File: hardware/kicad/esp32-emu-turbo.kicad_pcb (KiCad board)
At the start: 4 copper layers, 160 x 75 mm, 88 parts, among them J1 USB-C-16P, J3 JST-PH-2P-SMD, J4 FPC-40P-0.5mm, SW1 SW-SMD-5.1x5.1, SW10 SW-SMD-5.1x5.1, SW11 SW-SMD-5.1x5.1, SW12 SW-SMD-5.1x5.1, SW13 SW-SMD-5.1x5.1, SW2 SW-SMD-5.1x5.1, SW3 SW-SMD-5.1x5.1, SW4 SW-SMD-5.1x5.1, SW5 SW-SMD-5.1x5.1, SW6 SW-SMD-5.1x5.1, SW7 SW-SMD-5.1x5.1, SW8 SW-SMD-5.1x5.1, SW9 SW-SMD-5.1x5.1, U1 ESP32-S3-WROOM-1-N16R8, U2 ESOP-8, U3 SOT-223, U4 SOT-23-6, U5 SOP-16, U6 TF-01A

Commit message: feat(pcb+fw): add BAT54C menu combo diode — SW13 triggers START+SELECT
Hardware: D1 BAT54C dual Schottky (SOT-23, C8655) connects SW13 menu
button to BTN_START and BTN_SELECT via diode isolation. Pressing SW13
pulls both signals LOW simultaneously; firmware detects combo as MENU.
Includes SOT-23-3 footprint, MENU_K cathode net, routing, BOM/CPL/gerbers.

Firmware: BTN_MENU_COMBO macro + input_menu_pressed() combo detector.

Fixes: BTN_R jog clearance for SW13 GND pads, U5 VREF datasheet spec,
BTN_MENU orphan net in design-intent checker.

DFM: 115/115 pass, DFA: 9/9 pass, design intent: 363/363 pass.

Co-Authored-By: Claude Opus 4.6 (1M context) <noreply@anthropic.com>
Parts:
- removed the C26 at (91.5, 21.0)
- removed the C3 at (69.5, 42.0)
- removed the C4 at (92.0, 42.0)
- removed the J3 at (80.0, 62.5)
- removed the R17 at (25.0, 65.0)
- removed the R18 at (32.0, 65.0)
- removed the R22 at (90.2, 40.0)
- removed the R23 at (91.7, 38.5)
- removed the R3 at (65.0, 42.0)
- removed the SW7 at (142.0, 42.5)
- added C1: C_0805, C_0805, B.Cu at (120.0, 57.0)
- added C2: C_1206, C_1206, B.Cu at (125.0, 62.5)
- added C21: C_0805, C_0805, B.Cu at (38.0, 23.5)
- added C22: C_0805, C_0805, B.Cu at (33.2, 20.0)
- added C23: C_0805, C_0805, B.Cu at (38.0, 29.5)
- added C24: C_0805, C_0805, B.Cu at (29.4, 22.0)
- added C25: C_0805, C_0805, B.Cu at (31.5, 37.5)
- added D1: SOT-23-3, SOT-23-3, B.Cu at (156.0, 52.5)
- added FID3: Fiducial, Fiducial, F.Cu at (12.0, 63.0)
- added LED1: LED_0805, LED_0805, F.Cu at (25.0, 67.5)
- added R21: R_0805, R_0805, B.Cu at (38.0, 32.5)
- C11: renamed from C19; value C_1206 -> C_0805; footprint C_1206 -> C_0805
- C14: renamed from R20; value R_0805 -> C_0805; footprint R_0805 -> C_0805
- C15: renamed from R21; value R_0805 -> C_0805; footprint R_0805 -> C_0805
- C19: renamed from C1; value C_0805 -> C_1206; footprint C_0805 -> C_1206
- C26: renamed from R10; value R_0805 -> C_0805; footprint R_0805 -> C_0805
- C27: renamed from C2; value C_1206 -> C_0805; footprint C_1206 -> C_0805
- C3: renamed from R8; value R_0805 -> C_0805; footprint R_0805 -> C_0805
- C4: renamed from R9; value R_0805 -> C_0805; footprint R_0805 -> C_0805
- J3: renamed from U4; value SOT-23-6 -> JST-PH-2P-SMD; footprint SOT-23-6 -> JST-PH-2P-SMD
- R10: renamed from C6; value C_0805 -> R_0805; footprint C_0805 -> R_0805
- R11: renamed from C7; value C_0805 -> R_0805; footprint C_0805 -> R_0805
- R12: renamed from C8; value C_0805 -> R_0805; footprint C_0805 -> R_0805
- R13: renamed from C9; value C_0805 -> R_0805; footprint C_0805 -> R_0805
- R14: renamed from C10; value C_0805 -> R_0805; footprint C_0805 -> R_0805
- R15: renamed from C11; value C_0805 -> R_0805; footprint C_0805 -> R_0805
- R16: renamed from C13; value C_0805 -> R_0805; footprint C_0805 -> R_0805
- R19: renamed from C12; value C_0805 -> R_0805; footprint C_0805 -> R_0805
- R20: renamed from FID3; value Fiducial -> R_0805; footprint Fiducial -> R_0805; moved to B.Cu
- R22: renamed from R5; value R_0805 -> R_0402; footprint R_0805 -> R_0402
- R23: renamed from R6; value R_0805 -> R_0402; footprint R_0805 -> R_0402
- R9: renamed from C5; value C_0805 -> R_0805; footprint C_0805 -> R_0805
- SW7: renamed from LED1; value LED_0805 -> SW-SMD-5.1x5.1; footprint LED_0805 -> SW-SMD-5.1x5.1
- U4: renamed from R4; value R_0805 -> SOT-23-6; footprint R_0805 -> SOT-23-6
- moved SW7 119.6 mm to (142.0, 42.5)
- moved C18 85.3 mm to (116.0, 49.0)
- moved C17 81.7 mm to (110.0, 35.0)
- moved C20 68.2 mm to (103.0, 50.0)
- moved C16 65.6 mm to (98.0, 50.0)
- moved C13 58.2 mm to (83.0, 50.0)
- moved C15 57.7 mm to (93.0, 50.0)
- moved R17 56.3 mm to (25.0, 65.0)
- moved C14 55.2 mm to (88.0, 50.0)
- moved R18 54.4 mm to (32.0, 65.0)
- moved R8 52.4 mm to (63.0, 46.0)
- moved U4 50.0 mm to (91.0, 60.0)
- moved C9 49.3 mm to (63.0, 50.0)
- moved C10 48.0 mm to (68.0, 50.0)
- moved C5 45.0 mm to (43.0, 50.0)
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- renumbered C18 to C10, C27 to C12, C22 to C13, C21 to C16, C24 to C17, C25 to C18, C23 to C20, C14 to C5, C15 to C6, C16 to C7, C20 to C8, C17 to C9, R11 to R17, R12 to R18, R7 to R3, R13 to R4, R14 to R5, R15 to R6, R19 to R7, R16 to R8
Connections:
- C10 pad 1: BAT+ -> (no net)
- C10 pad 2: GND -> (no net)
- C11 pad 1: +5V -> (no net)
- C11 pad 2: GND -> (no net)
- C12 pad 1: GND -> (no net)
- C12 pad 2: +5V -> (no net)
- C13 pad 1: I2S_DOUT -> (no net)
- C13 pad 2: I2S_DOUT -> (no net)
- C14 pad 1: GND -> (no net)
- C14 pad 2: I2S_DOUT -> (no net)
- C15 pad 1: GND -> (no net)
- C15 pad 2: I2S_DOUT -> (no net)
- C16 pad 1: GND -> (no net)
- C16 pad 2: PAM_VREF -> (no net)
- C17 pad 1: GND -> VBUS
- C17 pad 2: +5V -> GND
- C18 pad 1: +5V -> BAT+
- C20 pad 1: +5V -> (no net)
- C20 pad 2: GND -> (no net)
- C26 pad 1: (no net) -> +3V3
- C26 pad 2: (no net) -> GND
- C27 pad 1: +3V3 -> GND
- C27 pad 2: GND -> +5V
- C3 pad 1: (no net) -> +3V3
- C3 pad 2: (no net) -> GND
- C4 pad 1: (no net) -> +3V3
- C4 pad 2: (no net) -> GND
- C9 pad 1: VBUS -> (no net)
- C9 pad 2: GND -> (no net)
- J3 pad 1: USB_D- -> BAT+
- R16 pad 1: (no net) -> +5V
- R16 pad 2: (no net) -> IP5306_KEY
- R17 pad 1: (no net) -> LED1_RA
- R17 pad 2: (no net) -> +3V3
- R18 pad 1: (no net) -> LED2_RA
- R18 pad 2: (no net) -> +3V3
- R20 pad 1: (no net) -> GND
- R22 pad 1: (no net) -> USB_DP_MCU
- R22 pad 2: (no net) -> USB_D+
- R23 pad 1: (no net) -> USB_DM_MCU
- R23 pad 2: (no net) -> USB_D-
- R8 pad 1: +5V -> (no net)
- R8 pad 2: IP5306_KEY -> (no net)
- SW13 pad 1: (no net) -> MENU_K
- SW13 pad 2: (no net) -> MENU_K
- SW13 pad 3: (no net) -> GND
- SW13 pad 4: (no net) -> GND
- SW7 pad 1: GND -> BTN_X
- SW7 pad 2: LED1_RA -> (no net)
- U4 pad 1: (no net) -> USB_D-
- U4 pad 2: (no net) -> GND
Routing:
- net MENU_K: track 0.00 -> 19.5 mm, vias 0 -> 1
- net GND: track 171.5 -> 183.4 mm, vias 78 -> 80
- net BTN_START: track 171.8 -> 174.3 mm, vias 5 -> 6
- net BTN_SELECT: track 109.0 -> 111.5 mm, vias 6 -> 7
- net BTN_R: track 178.1 -> 177.1 mm
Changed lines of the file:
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@@
   (net 54 "USB_DP_MCU")
   (net 55 "USB_DM_MCU")
+  (net 56 "MENU_K")
   (gr_line (start 6.0 0) (end 154.0 0) (stroke (width 0.05) (type default)) (layer "Edge.Cuts"))
   (gr_line (start 160.0 6.0) (end 160.0 69.0) (stroke (width 0.05) (type default)) (layer "Edge.Cuts"))
@@
     (property "Reference" "SW13" (at 0 -3 0) (layer "F.Fab") (effects (font (size 1 1) (thickness 0.2))))
     (property "Value" "SW-SMD-5.1x5.1" (at 0 3 0) (layer "F.Fab") (effects (font (size 1 1) (thickness 0.2))))
-    (pad "1" smd rect (at -3.0 -1.85) (size 1.0 0.7) (layers "F.Cu" "F.Paste" "F.Mask") (net 0 ""))
-    (pad "2" smd rect (at 3.0 -1.85) (size 1.0 0.7) (layers "F.Cu" "F.Paste" "F.Mask") (net 0 ""))
-    (pad "3" smd rect (at -3.0 1.85) (size 1.0 0.7) (layers "F.Cu" "F.Paste" "F.Mask") (net 0 ""))
-    (pad "4" smd rect (at 3.0 1.85) (size 1.0 0.7) (layers "F.Cu" "F.Paste" "F.Mask") (net 0 ""))
+    (pad "1" smd rect (at -3.0 -1.85) (size 1.0 0.7) (layers "F.Cu" "F.Paste" "F.Mask") (net 56 "MENU_K"))
+    (pad "2" smd rect (at 3.0 -1.85) (size 1.0 0.7) (layers "F.Cu" "F.Paste" "F.Mask") (net 56 "MENU_K"))
+    (pad "3" smd rect (at -3.0 1.85) (size 1.0 0.7) (layers "F.Cu" "F.Paste" "F.Mask") (net 1 "GND"))
+    (pad "4" smd rect (at 3.0 1.85) (size 1.0 0.7) (layers "F.Cu" "F.Paste" "F.Mask") (net 1 "GND"))
   )
   (footprint "LED_0805" (at 25.0 67.5) (layer "F.Cu")
@@
     (pad "3" smd rect (at 3.0 1.85) (size 1.0 0.7) (layers "B.Cu" "B.Paste" "B.Mask") (net 1 "GND"))
     (pad "4" smd rect (at -3.0 1.85) (size 1.0 0.7) (layers "B.Cu" "B.Paste" "B.Mask") (net 1 "GND"))
+  )
+  (footprint "SOT-23-3" (at 156.0 52.5) (layer "B.Cu")
+    (property "Reference" "D1" (at 0 -3 0) (layer "B.Fab") (effects (font (size 1 1) (thickness 0.2)) (justify mirror)))
+    (property "Value" "SOT-23-3" (at 0 3 0) (layer "B.Fab") (effects (font (size 1 1) (thickness 0.2)) (justify mirror)))
+    (pad "1" smd rect (at 0.95 1.1) (size 0.6 0.7) (layers "B.Cu" "B.Paste" "B.Mask") (net 35 "BTN_START"))
+    (pad "2" smd rect (at -0.95 1.1) (size 0.6 0.7) (layers "B.Cu" "B.Paste" "B.Mask") (net 36 "BTN_SELECT"))
+    (pad "3" smd rect (at 0.0 -1.1) (size 0.6 0.7) (layers "B.Cu" "B.Paste" "B.Mask") (net 56 "MENU_K"))
   )
   (footprint "R_0805" (at 74.0 67.0) (layer "B.Cu")
@@
   (via (at 146.85 65.29) (size 0.6) (drill 0.2) (layers "F.Cu" "B.Cu") (net 38))
   (segment (start 146.85 65.29) (end 146.5 65.29) (width 0.2) (layer "F.Cu") (net 38))
-  (segment (start 146.5 65.29) (end 146.5 64.0) (width 0.2) (layer "F.Cu") (net 38))
-  (segment (start 146.5 64.0) (end 137.0 64.0) (width 0.2) (layer "F.Cu") (net 38))
-  (segment (start 137.0 64.0) (end 137.0 65.29) (width 0.2) (layer "F.Cu") (net 38))
+  (segment (start 146.5 65.29) (end 146.5 64.5) (width 0.2) (layer "F.Cu") (net 38))
+  (segment (start 146.5 64.5) (end 137.0 64.5) (width 0.2) (layer "F.Cu") (net 38))
+  (segment (start 137.0 64.5) (end 137.0 65.29) (width 0.2) (layer "F.Cu") (net 38))
   (segment (start 137.0 65.29) (end 76.2 65.29) (width 0.2) (layer "F.Cu") (net 38))
   (via (at 76.2 65.29) (size 0.6) (drill 0.2) (layers "F.Cu" "B.Cu") (net 38))
@@
   (segment (start 102.0 63.65) (end 102.0 60.0) (width 0.25) (layer "B.Cu") (net 36))
   (via (at 102.0 60.0) (size 0.6) (drill 0.2) (layers "F.Cu" "B.Cu") (net 36))
+  (via (at 156.0 51.4) (size 0.6) (drill 0.2) (layers "F.Cu" "B.Cu") (net 56))
+  (segment (start 156.0 51.4) (end 156.0 59.85) (width 0.25) (layer "F.Cu") (net 56))
+  (segment (start 156.0 59.85) (end 145.0 59.85) (width 0.25) (layer "F.Cu") (net 56))
+  (segment (start 139.0 63.550000000000004) (end 135.0 63.550000000000004) (width 0.3) (layer "F.Cu") (net 1))
+  (segment (start 135.0 63.550000000000004) (end 135.0 61.550000000000004) (width 0.3) (layer "F.Cu") (net 1))
+  (via (at 135.0 61.550000000000004) (size 0.6) (drill 0.2) (layers "F.Cu" "B.Cu") (net 1))
+  (segment (start 145.0 63.550000000000004) (end 148.0 63.550000000000004) (width 0.3) (layer "F.Cu") (net 1))
+  (segment (start 148.0 63.550000000000004) (end 148.0 66.5) (width 0.3) (layer "F.Cu") (net 1))
+  (via (at 148.0 66.5) (size 0.6) (drill 0.2) (layers "F.Cu" "B.Cu") (net 1))
+  (segment (start 156.95 53.6) (end 156.95 56.1) (width 0.25) (layer "B.Cu") (net 35))
+  (via (at 156.95 56.1) (size 0.6) (drill 0.2) (layers "F.Cu" "B.Cu") (net 35))
+  (segment (start 155.05 53.6) (end 155.05 51.1) (width 0.25) (layer "B.Cu") (net 36))
+  (via (at 155.05 51.1) (size 0.6) (drill 0.2) (layers "F.Cu" "B.Cu") (net 36))
   (zone
     (net 1)

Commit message: fix(pcb): add USB return path GND vias + fix polarity test coverage
- Add 2 GND stitching vias at (86,69) and (88,69) near USB D+ serpentine
  to ensure all USB segments are within 5mm of a GND via (was 7.6mm max)
- Fix verify_polarity: SW13 net expectation MENU_K (was BTN_MENU)
- Fix verify_polarity: add D1 (BAT54C) net coverage for component check

Co-Authored-By: Claude Opus 4.6 (1M context) <noreply@anthropic.com>
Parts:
- removed the C2 at (125.0, 62.5)
- added FID3: Fiducial, Fiducial, F.Cu at (12.0, 63.0)
- C2: renamed from FID1; value Fiducial -> C_1206; footprint Fiducial -> C_1206; moved to B.Cu
- moved FID1 147.1 mm to (12.0, 12.0)
- moved FID2 138.0 mm to (150.0, 63.0)
- moved C2 123.8 mm to (125.0, 62.5)
- renumbered FID2 to FID1, FID3 to FID2
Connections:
- C2 pad 1: (no net) -> +3V3
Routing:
- net GND: vias 80 -> 82
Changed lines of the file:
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@@
   (segment (start 77.05 67.0) (end 77.05 63.8) (width 0.3) (layer "B.Cu") (net 1))
   (via (at 77.05 63.8) (size 0.6) (drill 0.2) (layers "F.Cu" "B.Cu") (net 1))
+  (via (at 86.0 69.0) (size 0.6) (drill 0.2) (layers "F.Cu" "B.Cu") (net 1))
+  (via (at 88.0 69.0) (size 0.6) (drill 0.2) (layers "F.Cu" "B.Cu") (net 1))
   (segment (start 21.0 21.65) (end 22.2 21.65) (width 0.25) (layer "F.Cu") (net 27))
   (via (at 22.2 21.65) (size 0.5) (drill 0.2) (layers "F.Cu" "B.Cu") (net 27))

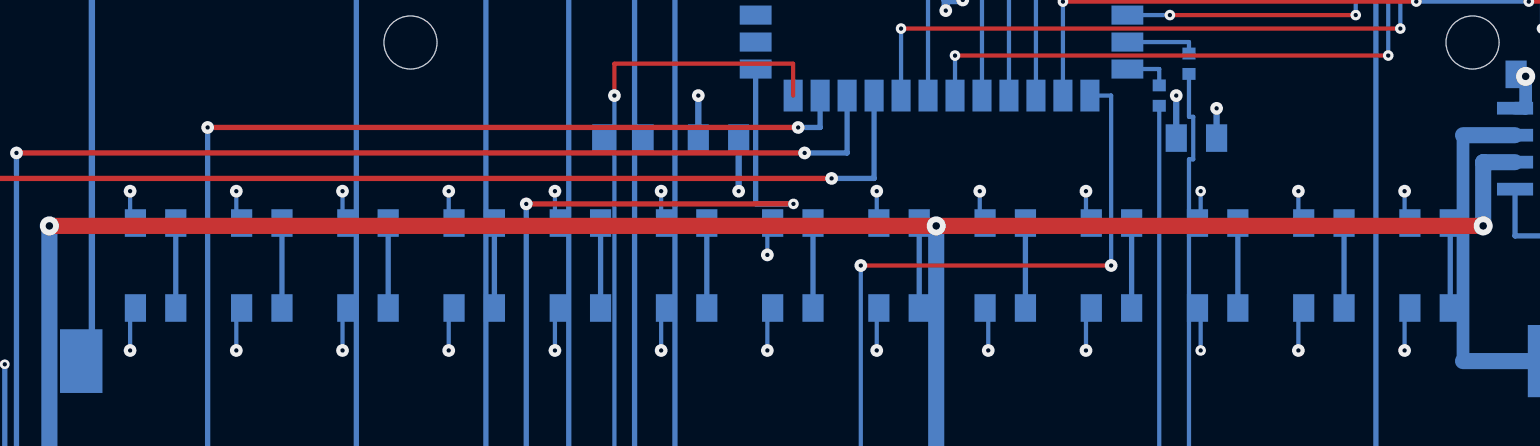
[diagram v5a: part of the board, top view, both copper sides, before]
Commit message: fix: eliminate 14 warnings — I2S pad nets, pull-up checker, +3V3 stubs
- Assign I2S_BCLK/LRCK nets to U1 pads 8/9 (GPIO15/16) — eliminates
  2 "no pad assignment" warnings in T14 and T5
- Rewrite T17 pull-up checker: verify R4-R15/R19 (13 resistors) and
  C5-C16/C20 (13 debounce caps) exist in PCB — eliminates 12 false
  "no discrete pull-up" warnings (pull-ups are on separate network)
- Widen +3V3 pull-up stubs from 0.2mm to 0.25mm — reduces JLCPCB
  power trace warnings from 52 to 26 segments

Result: 358 PASS / 0 FAIL / 3 WARN (was 17 WARN)

Co-Authored-By: Claude Opus 4.6 (1M context) <noreply@anthropic.com>
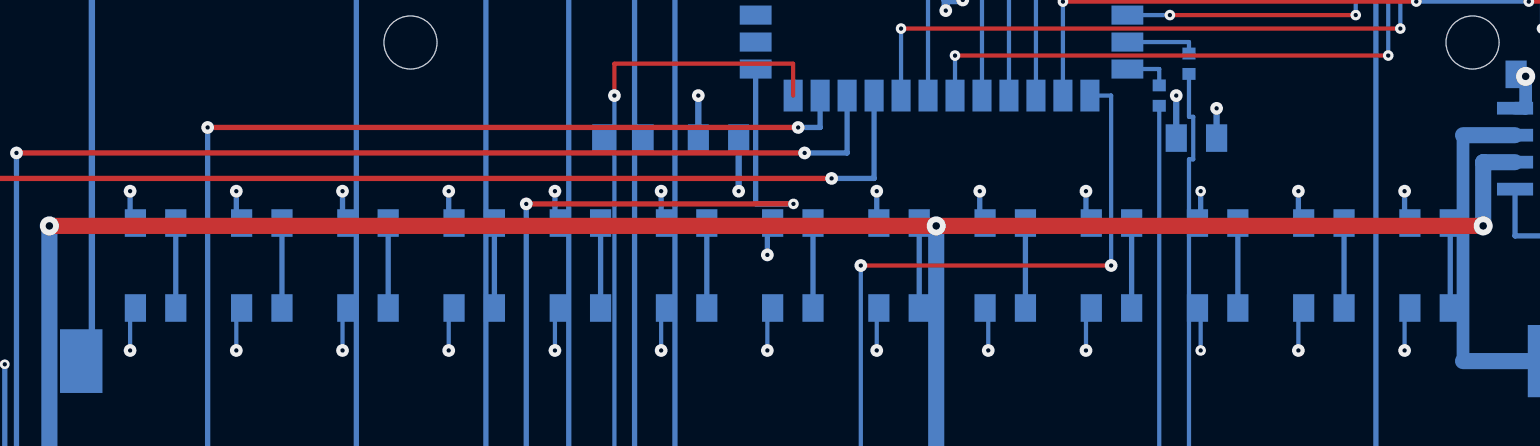
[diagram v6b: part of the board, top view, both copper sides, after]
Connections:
- U1 pad 8: (no net) -> I2S_BCLK
- U1 pad 9: (no net) -> I2S_LRCK
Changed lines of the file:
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@@
     (pad "6" smd rect (at 8.75 1.0899999999999999) (size 1.5 0.9) (layers "B.Cu" "B.Paste" "B.Mask") (net 8 "LCD_D2"))
     (pad "7" smd rect (at 8.75 2.3600000000000003) (size 1.5 0.9) (layers "B.Cu" "B.Paste" "B.Mask") (net 9 "LCD_D3"))
-    (pad "8" smd rect (at 8.75 3.630000000000001) (size 1.5 0.9) (layers "B.Cu" "B.Paste" "B.Mask") (net 0 ""))
-    (pad "9" smd rect (at 8.75 4.9) (size 1.5 0.9) (layers "B.Cu" "B.Paste" "B.Mask") (net 0 ""))
+    (pad "8" smd rect (at 8.75 3.630000000000001) (size 1.5 0.9) (layers "B.Cu" "B.Paste" "B.Mask") (net 24 "I2S_BCLK"))
+    (pad "9" smd rect (at 8.75 4.9) (size 1.5 0.9) (layers "B.Cu" "B.Paste" "B.Mask") (net 25 "I2S_LRCK"))
     (pad "10" smd rect (at 8.75 6.17) (size 1.5 0.9) (layers "B.Cu" "B.Paste" "B.Mask") (net 26 "I2S_DOUT"))
     (pad "11" smd rect (at 8.75 7.4399999999999995) (size 1.5 0.9) (layers "B.Cu" "B.Paste" "B.Mask") (net 35 "BTN_START"))
@@
   (segment (start 143.15 8.5) (end 144.65 8.5) (width 0.3) (layer "B.Cu") (net 1))
   (via (at 144.65 8.5) (size 0.6) (drill 0.2) (layers "F.Cu" "B.Cu") (net 1))
-  (segment (start 42.05 46) (end 41.8 46) (width 0.2) (layer "B.Cu") (net 4))
-  (segment (start 41.8 46) (end 41.8 44.5) (width 0.2) (layer "B.Cu") (net 4))
+  (segment (start 42.05 46) (end 41.8 46) (width 0.25) (layer "B.Cu") (net 4))
+  (segment (start 41.8 46) (end 41.8 44.5) (width 0.25) (layer "B.Cu") (net 4))
   (via (at 41.8 44.5) (size 0.6) (drill 0.2) (layers "F.Cu" "B.Cu") (net 4))
-  (segment (start 47.05 46) (end 46.8 46) (width 0.2) (layer "B.Cu") (net 4))
-  (segment (start 46.8 46) (end 46.8 44.5) (width 0.2) (layer "B.Cu") (net 4))
+  (segment (start 47.05 46) (end 46.8 46) (width 0.25) (layer "B.Cu") (net 4))
+  (segment (start 46.8 46) (end 46.8 44.5) (width 0.25) (layer "B.Cu") (net 4))
   (via (at 46.8 44.5) (size 0.6) (drill 0.2) (layers "F.Cu" "B.Cu") (net 4))
-  (segment (start 52.05 46) (end 51.8 46) (width 0.2) (layer "B.Cu") (net 4))
-  (segment (start 51.8 46) (end 51.8 44.5) (width 0.2) (layer "B.Cu") (net 4))
+  (segment (start 52.05 46) (end 51.8 46) (width 0.25) (layer "B.Cu") (net 4))
+  (segment (start 51.8 46) (end 51.8 44.5) (width 0.25) (layer "B.Cu") (net 4))
   (via (at 51.8 44.5) (size 0.6) (drill 0.2) (layers "F.Cu" "B.Cu") (net 4))
-  (segment (start 57.05 46) (end 56.8 46) (width 0.2) (layer "B.Cu") (net 4))
-  (segment (start 56.8 46) (end 56.8 44.5) (width 0.2) (layer "B.Cu") (net 4))
+  (segment (start 57.05 46) (end 56.8 46) (width 0.25) (layer "B.Cu") (net 4))
+  (segment (start 56.8 46) (end 56.8 44.5) (width 0.25) (layer "B.Cu") (net 4))
   (via (at 56.8 44.5) (size 0.6) (drill 0.2) (layers "F.Cu" "B.Cu") (net 4))
-  (segment (start 62.05 46) (end 61.8 46) (width 0.2) (layer "B.Cu") (net 4))
-  (segment (start 61.8 46) (end 61.8 44.5) (width 0.2) (layer "B.Cu") (net 4))
+  (segment (start 62.05 46) (end 61.8 46) (width 0.25) (layer "B.Cu") (net 4))
+  (segment (start 61.8 46) (end 61.8 44.5) (width 0.25) (layer "B.Cu") (net 4))
   (via (at 61.8 44.5) (size 0.6) (drill 0.2) (layers "F.Cu" "B.Cu") (net 4))
-  (segment (start 67.05 46) (end 66.8 46) (width 0.2) (layer "B.Cu") (net 4))
-  (segment (start 66.8 46) (end 66.8 44.5) (width 0.2) (layer "B.Cu") (net 4))
+  (segment (start 67.05 46) (end 66.8 46) (width 0.25) (layer "B.Cu") (net 4))
+  (segment (start 66.8 46) (end 66.8 44.5) (width 0.25) (layer "B.Cu") (net 4))
   (via (at 66.8 44.5) (size 0.6) (drill 0.2) (layers "F.Cu" "B.Cu") (net 4))
-  (segment (start 72.05 46) (end 71.8 46) (width 0.2) (layer "B.Cu") (net 4))
-  (segment (start 71.8 46) (end 71.8 47.5) (width 0.2) (layer "B.Cu") (net 4))
+  (segment (start 72.05 46) (end 71.8 46) (width 0.25) (layer "B.Cu") (net 4))
+  (segment (start 71.8 46) (end 71.8 47.5) (width 0.25) (layer "B.Cu") (net 4))
   (via (at 71.8 47.5) (size 0.6) (drill 0.2) (layers "F.Cu" "B.Cu") (net 4))
-  (segment (start 77.05 46) (end 76.95 46) (width 0.2) (layer "B.Cu") (net 4))
-  (segment (start 76.95 46) (end 76.95 44.5) (width 0.2) (layer "B.Cu") (net 4))
+  (segment (start 77.05 46) (end 76.95 46) (width 0.25) (layer "B.Cu") (net 4))
+  (segment (start 76.95 46) (end 76.95 44.5) (width 0.25) (layer "B.Cu") (net 4))
   (via (at 76.95 44.5) (size 0.6) (drill 0.2) (layers "F.Cu" "B.Cu") (net 4))
-  (segment (start 82.05 46) (end 81.8 46) (width 0.2) (layer "B.Cu") (net 4))
-  (segment (start 81.8 46) (end 81.8 44.5) (width 0.2) (layer "B.Cu") (net 4))
+  (segment (start 82.05 46) (end 81.8 46) (width 0.25) (layer "B.Cu") (net 4))
+  (segment (start 81.8 46) (end 81.8 44.5) (width 0.25) (layer "B.Cu") (net 4))
   (via (at 81.8 44.5) (size 0.6) (drill 0.2) (layers "F.Cu" "B.Cu") (net 4))
-  (segment (start 87.05 46) (end 86.8 46) (width 0.2) (layer "B.Cu") (net 4))
-  (segment (start 86.8 46) (end 86.8 44.5) (width 0.2) (layer "B.Cu") (net 4))
+  (segment (start 87.05 46) (end 86.8 46) (width 0.25) (layer "B.Cu") (net 4))
+  (segment (start 86.8 46) (end 86.8 44.5) (width 0.25) (layer "B.Cu") (net 4))
   (via (at 86.8 44.5) (size 0.6) (drill 0.2) (layers "F.Cu" "B.Cu") (net 4))
-  (segment (start 92.05 46) (end 92.2 46) (width 0.2) (layer "B.Cu") (net 4))
-  (segment (start 92.2 46) (end 92.2 44.5) (width 0.2) (layer "B.Cu") (net 4))
+  (segment (start 92.05 46) (end 92.2 46) (width 0.25) (layer "B.Cu") (net 4))
+  (segment (start 92.2 46) (end 92.2 44.5) (width 0.25) (layer "B.Cu") (net 4))
   (via (at 92.2 44.5) (size 0.5) (drill 0.2) (layers "F.Cu" "B.Cu") (net 4))
-  (segment (start 97.05 46) (end 96.8 46) (width 0.2) (layer "B.Cu") (net 4))
-  (segment (start 96.8 46) (end 96.8 44.5) (width 0.2) (layer "B.Cu") (net 4))
+  (segment (start 97.05 46) (end 96.8 46) (width 0.25) (layer "B.Cu") (net 4))
+  (segment (start 96.8 46) (end 96.8 44.5) (width 0.25) (layer "B.Cu") (net 4))
   (via (at 96.8 44.5) (size 0.6) (drill 0.2) (layers "F.Cu" "B.Cu") (net 4))
-  (segment (start 102.05 46) (end 101.8 46) (width 0.2) (layer "B.Cu") (net 4))
-  (segment (start 101.8 46) (end 101.8 44.5) (width 0.2) (layer "B.Cu") (net 4))
+  (segment (start 102.05 46) (end 101.8 46) (width 0.25) (layer "B.Cu") (net 4))
+  (segment (start 101.8 46) (end 101.8 44.5) (width 0.25) (layer "B.Cu") (net 4))
   (via (at 101.8 44.5) (size 0.6) (drill 0.2) (layers "F.Cu" "B.Cu") (net 4))
   (segment (start 42.05 50) (end 41.8 50) (width 0.2) (layer "B.Cu") (net 1))
